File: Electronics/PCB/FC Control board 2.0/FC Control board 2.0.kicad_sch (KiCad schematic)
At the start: 76 parts, among them IC1 A3909GLNTR-T, IC2 A3909GLNTR-T, J1 USB_C_Receptacle_USB2.0, J2 CAM, J3 Servo, J4 Hall-M1, J5 Hall-M2, J6 Hall-M0, J7 Hall-M3, M0 Motor_DC_ALT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

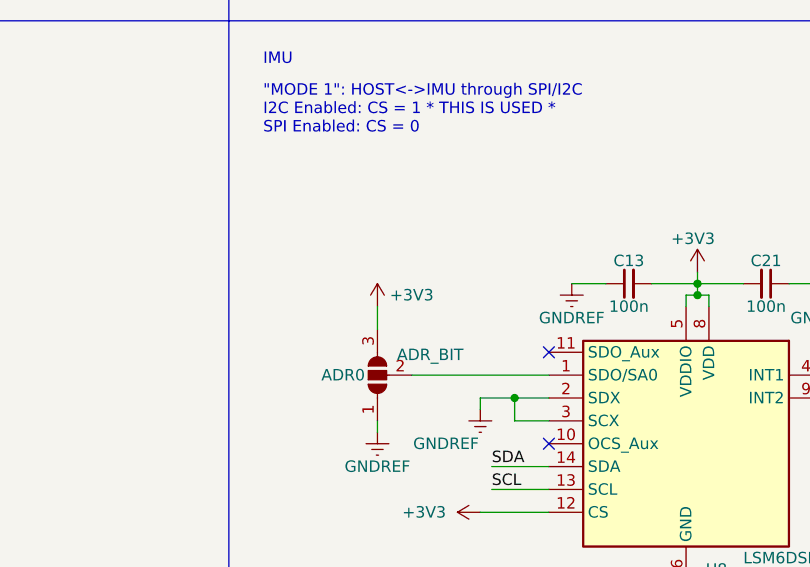
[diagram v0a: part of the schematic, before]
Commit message: FC 1.3 -> FC 2.0
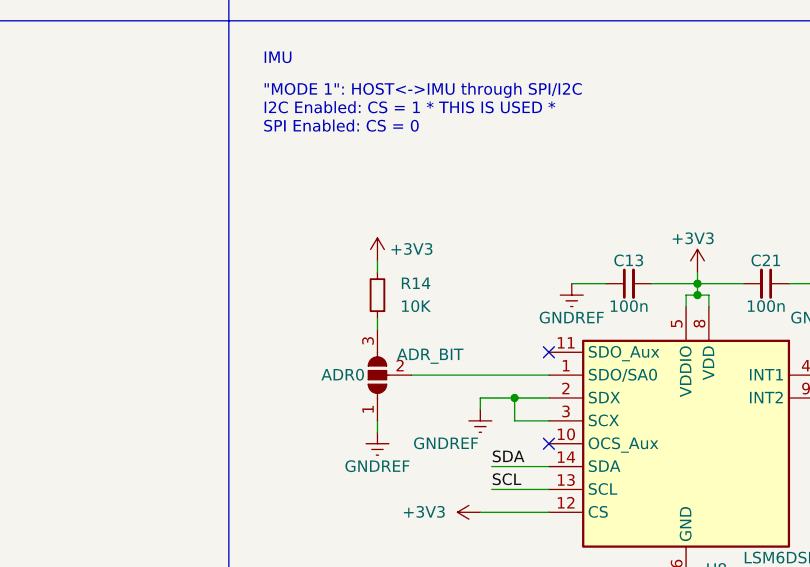
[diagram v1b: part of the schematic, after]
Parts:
- added R14: 10K, Resistor_SMD:R_0603_1608Metric_Pad0.98x0.95mm_HandSolder, symbol Device:R_Small
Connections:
- net +3V3: now also R14.2; no longer ADR0.3 (B)
- new net: ADR0.3 (B), R14.1

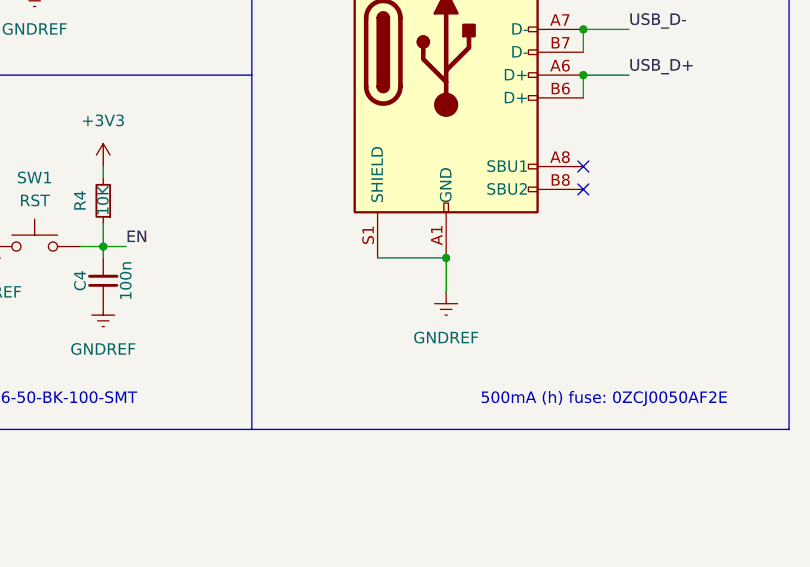
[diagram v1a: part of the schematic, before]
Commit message: Functioning 1.2 prototype
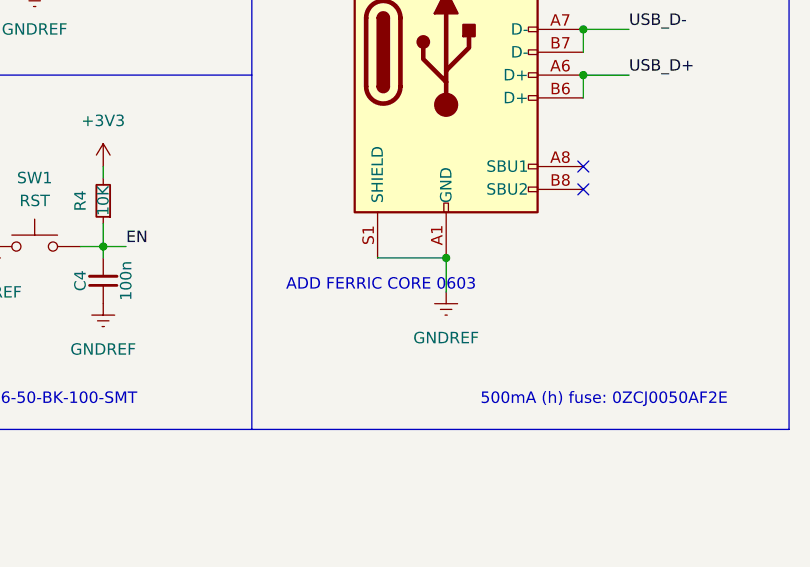
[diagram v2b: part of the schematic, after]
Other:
- note added: "ADD FERRIC CORE 0603"
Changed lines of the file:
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@@
+    (effects (font (size 1.27 1.27)) (justify left bottom))
+  )
+  (text "ADD FERRIC CORE 0603" (at 350.52 72.39 0)
     (effects (font (size 1.27 1.27)) (justify left bottom))
   )

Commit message: Add clamping diodes and opto couplers
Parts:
- added C20, C22: 100n, Capacitor_SMD:C_0603_1608Metric_Pad1.08x0.95mm_HandSolder, symbol Device:C
- added D7: HPZRC8V8QX, FC_footprint_library:HPZRC8V8QX, symbol Device:D_Zener
- added D8: PDZVTR36B, FC_footprint_library:PDZVTR36B, symbol Device:D_Zener
- added IC3, IC4: LTV-247, LTV247, symbol LTV-247:LTV-247
- added R15: R_PWM, Resistor_SMD:R_0603_1608Metric_Pad0.98x0.95mm_HandSolder, symbol Device:R_Small
- added R16: R_OPTO, Resistor_SMD:R_0603_1608Metric_Pad0.98x0.95mm_HandSolder, symbol Device:R_Small
- C1: value C -> 100n; footprint Capacitor_SMD:C_1206_3216Metric -> Capacitor_SMD:C_0603_1608Metric_Pad1.08x0.95mm_HandSolder
- C11, C17, C18, C9: value C_MAYBE -> 100n; footprint Capacitor_SMD:C_1206_3216Metric -> Capacitor_SMD:C_0603_1608Metric_Pad1.08x0.95mm_HandSolder
- U6: footprint INA4181A3IPWR:SOP65P640X120-20N -> FC_footprint_library:SOP65P640X120-20N
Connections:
- net +3V3: now also D8.1 (K), R16.2
- net FWR_0: now also IC3.1 (A_1); no longer U4.2 (1Z)
- net FWR_1: now also IC3.5 (A_3); no longer U4.10 (3Z)
- net FWR_2: now also IC4.1 (A_1); no longer U5.2 (1Z)
- net FWR_3: now also IC4.7 (A_4); no longer U5.10 (3Z)
- net GNDREF: now also C20.1, C22.1, D7.2 (A), D8.2 (A), R15.1
- net REV_0: now also IC3.3 (A_2); no longer U4.6 (2Z)
- net REV_1: now also IC3.7 (A_4); no longer U4.14 (4Z)
- net REV_2: now also IC4.3 (A_2); no longer U5.6 (2Z)
- net REV_3: now also IC4.5 (A_3); no longer U5.14 (4Z)
- net VCC: now also C20.2, C22.2, D7.1 (K)
- new net OPTO_3V3: IC3.10 (C_4), IC3.12 (C_3), IC3.14 (C_2), IC3.16 (C_1), IC4.10 (C_4), IC4.12 (C_3), IC4.14 (C_2), IC4.16 (C_1), R16.1
- new net OPTO_FWR_0: IC3.15 (E_1), U4.2 (1Z)
- new net OPTO_FWR_1: IC3.11 (E_3), U4.10 (3Z)
- new net OPTO_FWR_2: IC4.15 (E_1), U5.2 (1Z)
- new net OPTO_FWR_3: IC4.11 (E_3), U5.10 (3Z)
- new net OPTO_GND: IC3.2 (K_1), IC3.4 (K_2), IC3.6 (K_3), IC3.8 (K_4), IC4.2 (K_1), IC4.4 (K_2), IC4.6 (K_3), IC4.8 (K_4), R15.2
- new net OPTO_REV_0: IC3.13 (E_2), U4.6 (2Z)
- new net OPTO_REV_1: IC3.9 (E_4), U4.14 (4Z)
- new net OPTO_REV_2: IC4.13 (E_2), U5.6 (2Z)
- new net OPTO_REV_3: IC4.9 (E_4), U5.14 (4Z)
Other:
- note added: "1K?"
- note added: "3.6V (6%)"
- note added: "7.2-8.4V"
- note added: "8.8V (5%)"
- note added: "GPIO35 has weak pull up on reset, moved FWR_0 away"
- note added: "Optocoupler between ESP and logic input"
- note added: "Shared current limit resistors"
- note added: "Voltage clamping with zener diodes"
- note removed: "Weak pull up on reset, moved FWR_0 away"
- moved on the sheet: C12, C14, C15, C16, U4, U5

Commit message: Final version of 2.0 [Ordered]
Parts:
- U9: footprint Package_DFN_QFN:DFN-8-1EP_2x2mm_P0.5mm_EP1.05x1.75mm -> Package_SO:SOIC-8-1EP_3.9x4.9mm_P1.27mm_EP2.514x3.2mm
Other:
- moved on the sheet: BT1, D5, Q1, R10, R11, R8, R9, SW4
